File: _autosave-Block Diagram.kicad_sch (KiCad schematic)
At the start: 0 parts

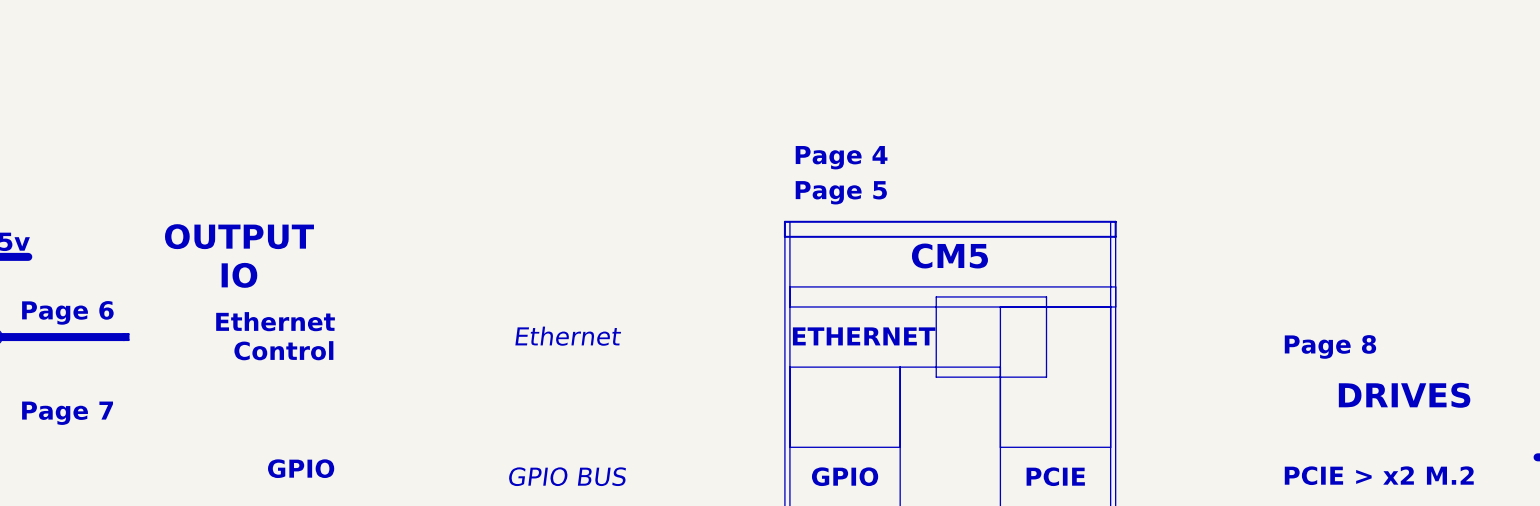
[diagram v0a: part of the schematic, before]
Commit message: CM5 IO done
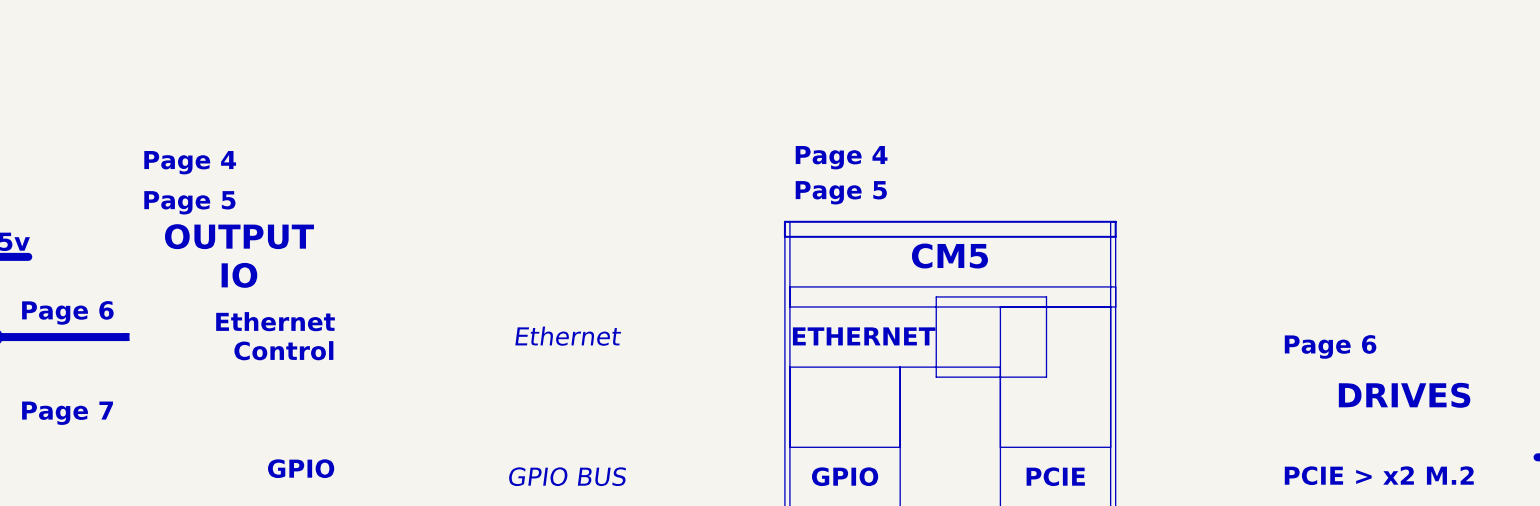
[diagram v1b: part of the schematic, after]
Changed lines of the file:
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@@
 		)
 	)
-	(text_box "Page 8"
+	(text_box "Page 6"
 		(exclude_from_sim no)
 		(at 302.006 97.028 0)
@@
 			)
 			(justify left top)
-			(href "#8")
+			(href "#6")
 		)
 	)
@@
 		)
 	)
+	(text_box "Page 5"
+		(exclude_from_sim no)
+		(at 157.48 78.74 0)
+		(size 24.765 5.08)
+		(margins 1.7144 1.7144 1.7144 1.7144)
+		(stroke
+			(width -0.0001)
+			(type default)
+		)
+		(fill
+			(type none)
+		)
+		(effects
+			(font
+				(face "Times New Roman")
+				(size 2.286 2.286)
+				(thickness 0.4572)
+				(bold yes)
+				(color 0 0 0 1)
+			)
+			(justify left top)
+			(href "#5")
+		)
+	)
 	(text_box "PCIE > x2 M.2"
 		(exclude_from_sim no)
@@
 				(color 0 0 0 1)
 			)
+			(justify left top)
+		)
+	)
+	(text_box "Page 4"
+		(exclude_from_sim no)
+		(at 157.48 73.66 0)
+		(size 24.765 5.08)
+		(margins 1.7144 1.7144 1.7144 1.7144)
+		(stroke
+			(width -0.0001)
+			(type default)
+		)
+		(fill
+			(type none)
+		)
+		(effects
+			(font
+				(face "Times New Roman")
+				(size 2.286 2.286)
+				(thickness 0.4572)
+				(bold yes)
+				(color 0 0 0 1)
+			)
